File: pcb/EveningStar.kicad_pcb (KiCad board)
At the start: 2 copper layers, 9 parts, among them Q1 SQ2308CES-T1_GE3, U3 ISO6721RBD, U4 ESP32-C6-MINI-1, U5 LMR16010, U6 TLV803S, U7 W5500

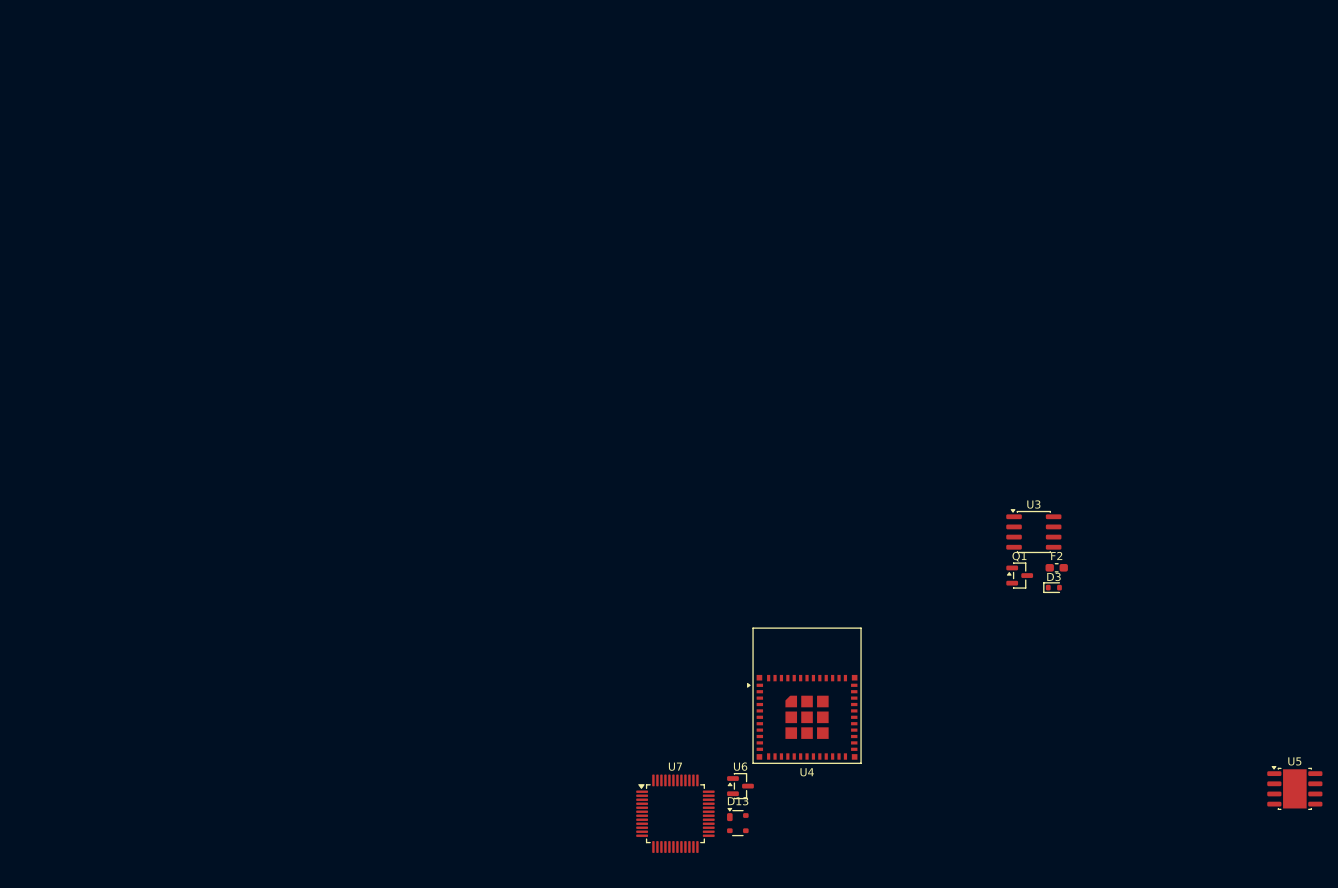
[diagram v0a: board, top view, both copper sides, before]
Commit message: feat: update compoents with lcsc parts
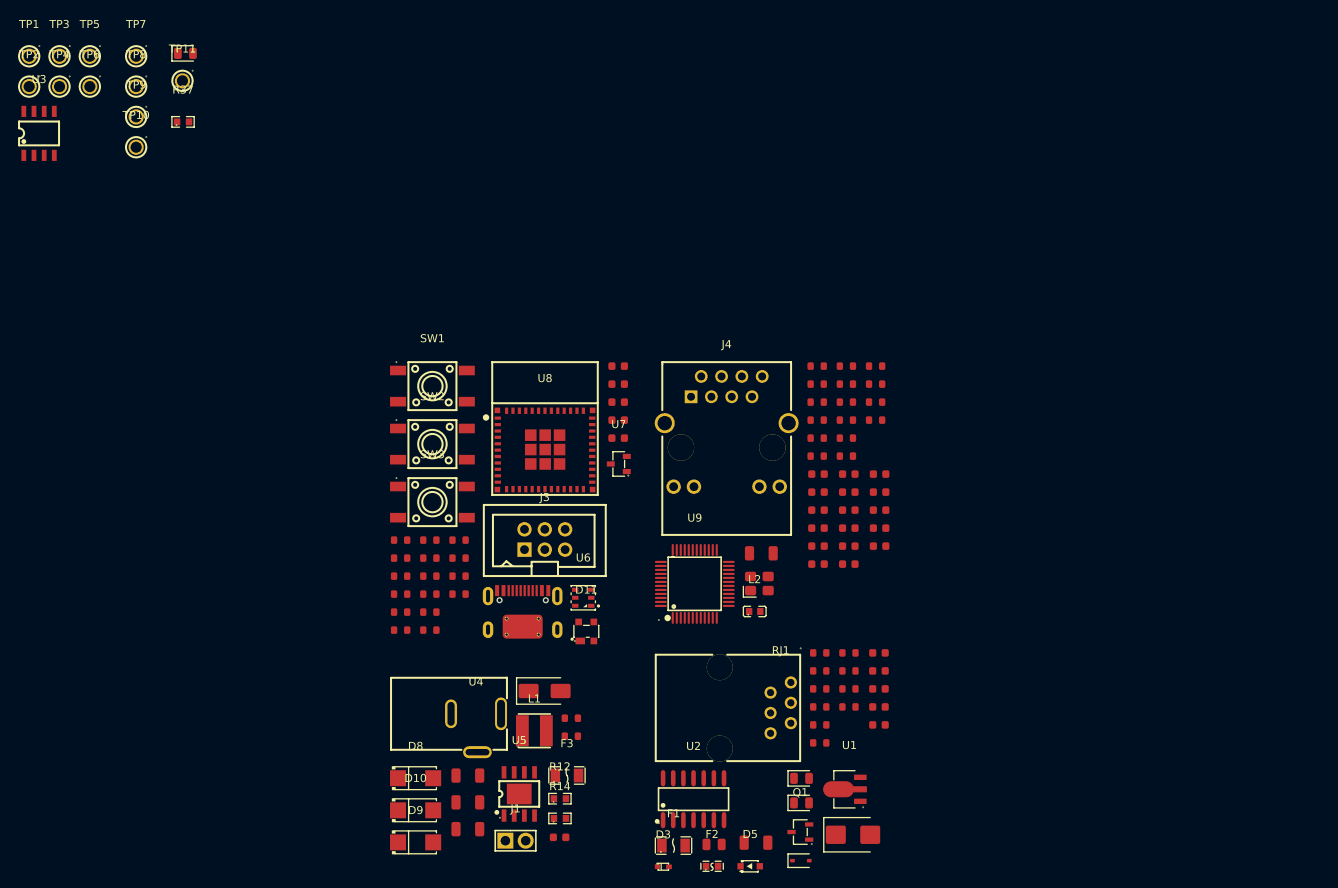
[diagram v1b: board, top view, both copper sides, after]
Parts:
- removed D13: PRTR5V0U2X, Package_TO_SOT_SMD:SOT-143
- added C1: 10uF, PCM_JLCPCB:C_1206, F.Cu at (92.2, 99.7)
- added C10: 100nF, PCM_JLCPCB:C_0603, F.Cu at (67.7, 99.0)
- added C11: 47uF, PCM_JLCPCB:C_1206, F.Cu at (56.2, 98.0)
- added C12: 100nF, PCM_JLCPCB:C_0603, F.Cu at (75.0, 44.6)
- added C13: 100nF, PCM_JLCPCB:C_0603, F.Cu at (75.0, 40.1)
- added C14: 100nF, PCM_JLCPCB:C_0603, F.Cu at (75.0, 42.4)
- added C15: 10uF, PCM_JLCPCB:C_0603, F.Cu at (75.0, 49.1)
- added C16: 100nF, PCM_JLCPCB:C_0603, F.Cu at (75.0, 46.9)
- added C17: 18pF, PCM_JLCPCB:C_0603, F.Cu at (100.0, 55.9)
- added C18: 18pF, PCM_JLCPCB:C_0603, F.Cu at (100.0, 53.6)
- added C19: 10uF, PCM_JLCPCB:C_0603, F.Cu at (107.7, 62.6)
- added C2: 330nF, PCM_JLCPCB:C_0805, F.Cu at (87.0, 99.9)
- added C20: 100nF, PCM_JLCPCB:C_0603, F.Cu at (100.0, 62.6)
- added C21: 1nF, PCM_JLCPCB:C_1206, F.Cu at (92.9, 63.5)
- added C22: 100nF, PCM_JLCPCB:C_0603, F.Cu at (100.0, 64.9)
- added C23: 10nF, PCM_JLCPCB:C_0603, F.Cu at (107.7, 55.9)
- added C24: 100nF, PCM_JLCPCB:C_0603, F.Cu at (103.8, 53.6)
- added C25: 4.7uF, PCM_JLCPCB:C_0603, F.Cu at (103.8, 55.9)
- added C26: 100nF, PCM_JLCPCB:C_0603, F.Cu at (103.8, 58.1)
- added C27: 100nF, PCM_JLCPCB:C_0603, F.Cu at (103.8, 62.6)
- added C28: 100nF, PCM_JLCPCB:C_0603, F.Cu at (103.8, 64.9)
- added C29: 10nF, PCM_JLCPCB:C_0603, F.Cu at (107.7, 60.4)
- added C3: 100nF, PCM_JLCPCB:C_0603, F.Cu at (107.6, 78.2)
- added C30: 100nF, PCM_JLCPCB:C_0603, F.Cu at (107.7, 53.6)
- added C31: 6.8nF, PCM_JLCPCB:C_0603, F.Cu at (107.7, 58.1)
- added C32: 6.8nF, PCM_JLCPCB:C_0603, F.Cu at (100.0, 60.4)
- added C33: 10uF, PCM_JLCPCB:C_0603, F.Cu at (103.8, 60.4)
- added C34: 22nF, PCM_JLCPCB:C_0603, F.Cu at (100.0, 58.1)
- added C4: 10uF, PCM_JLCPCB:C_0603, F.Cu at (107.6, 76.0)
- added C5: 100nF, PCM_JLCPCB:C_0603, F.Cu at (107.6, 80.5)
- added C6: 100nF, PCM_JLCPCB:C_0603, F.Cu at (107.6, 85.0)
- added C7: 100nF, PCM_JLCPCB:C_0603, F.Cu at (107.6, 82.7)
- added C8: 2.2uF, PCM_JLCPCB:C_1206, F.Cu at (56.2, 91.3)
- added C9: 2.2uF, PCM_JLCPCB:C_1206, F.Cu at (56.2, 94.7)
- added D1: SMBJ30CA, PCM_JLCPCB:D_SMB, F.Cu at (104.4, 98.7)
- added D10: STPS1H100A, EasyEDA:SMA_L4.3-W2.6-LS5.2-RD, F.Cu at (49.7, 95.6)
- added D11: PRTR5V0U2X_C2827688, EasyEDA:SOT-143-4_L2.9-W1.3-P1.92-LS2.4-BL, F.Cu at (71.0, 73.3)
- added D12: White, PCM_JLCPCB:D_0805, F.Cu at (20.9, 1.03)
- added D2: B16WS, PCM_JLCPCB:D_SOD-323, F.Cu at (97.9, 101.9)
- added D4: Red, PCM_JLCPCB:D_0805, F.Cu at (97.9, 94.7)
- added D5: BZX384-B5V1,115, EasyEDA:SOD-323_L1.7-W1.3-LS2.5-RD, F.Cu at (91.5, 102.6)
- added D6: Green, PCM_JLCPCB:D_0805, F.Cu at (97.9, 91.7)
- added D7: SMAJ28CA, PCM_JLCPCB:D_SMA, F.Cu at (65.8, 80.7)
- added D8: STPS1H100A, EasyEDA:SMA_L4.3-W2.6-LS5.2-RD, F.Cu at (49.7, 91.6)
- added D9: STPS1H100A, EasyEDA:SMA_L4.3-W2.6-LS5.2-RD, F.Cu at (49.7, 99.7)
- added F1: BSMD1206C-0500T, EasyEDA:F1206, F.Cu at (81.9, 100.1)
- added F3: 1A, EasyEDA:F1206, F.Cu at (68.6, 91.3)
- added J1: 3V3_JMP, EasyEDA:HDR-TH_2P-P2.54-V-M, F.Cu at (62.2, 99.5)
- added J2: Connector, USB-TYPE-C-16P, PCM_JLCPCB:TYPE-C-SMD_HX-TYPE-C-16PIN, F.Cu at (63.1, 70.7)
- added J3: ESPPROG, EasyEDA:IDC-TH_6P-P2.54-V-R2-C3-S2.54, F.Cu at (65.8, 61.8)
- added J4: RJ45_Hanrun_HR911105A_Horizontal, EasyEDA:RJ45-TH_HR911105A, F.Cu at (88.6, 48.3)
- added L1: 10uH, EasyEDA:IND-SMD_L4.0-W4.0_FNR40XXS, F.Cu at (64.5, 85.7)
- added L2: BLM18PG121SN1D_C14709, EasyEDA:L0603, F.Cu at (92.1, 70.8)
- added R1: 100Ω, PCM_JLCPCB:R_0603, F.Cu at (100.2, 87.2)
- added R10: 10kΩ, PCM_JLCPCB:R_0603, F.Cu at (103.9, 80.5)
- added R11: 10kΩ, PCM_JLCPCB:R_0603, F.Cu at (69.2, 84.1)
- added R12: 34.8k, EasyEDA:R0603, F.Cu at (67.7, 94.2)
- added R13: 100kΩ, PCM_JLCPCB:R_0603, F.Cu at (69.2, 86.4)
- added R14: 29.4k, EasyEDA:R0603, F.Cu at (67.7, 96.7)
- added R15: 10kΩ, PCM_JLCPCB:R_0603, F.Cu at (47.8, 73.1)
- added R16: 10kΩ, PCM_JLCPCB:R_0603, F.Cu at (51.5, 61.9)
- added R17: 10kΩ, PCM_JLCPCB:R_0603, F.Cu at (51.5, 70.9)
- added R18: 5.1kΩ, PCM_JLCPCB:R_0603, F.Cu at (47.8, 61.9)
- added R19: 5.1kΩ, PCM_JLCPCB:R_0603, F.Cu at (47.8, 64.1)
- added R2: 1MΩ, PCM_JLCPCB:R_0603, F.Cu at (100.2, 76.0)
- added R20: 10kΩ, PCM_JLCPCB:R_0603, F.Cu at (51.5, 73.1)
- added R21: 10kΩ, PCM_JLCPCB:R_0603, F.Cu at (55.1, 61.9)
- added R22: 220Ω, PCM_JLCPCB:R_0603, F.Cu at (47.8, 66.4)
- added R23: 33Ω, PCM_JLCPCB:R_0603, F.Cu at (47.8, 68.6)
- added R24: 33Ω, PCM_JLCPCB:R_0603, F.Cu at (47.8, 70.9)
- added R25: 33Ω, PCM_JLCPCB:R_0603, F.Cu at (51.5, 64.1)
- added R26: 33Ω, PCM_JLCPCB:R_0603, F.Cu at (51.5, 66.4)
- added R27: 33Ω, PCM_JLCPCB:R_0603, F.Cu at (51.5, 68.6)
- added R28: 10kΩ, PCM_JLCPCB:R_0603, F.Cu at (55.1, 64.1)
- added R29: 10kΩ, PCM_JLCPCB:R_0603, F.Cu at (55.1, 66.4)
- added R3: 100kΩ, PCM_JLCPCB:R_0603, F.Cu at (103.9, 78.2)
- added R30: 10kΩ, PCM_JLCPCB:R_0603, F.Cu at (55.1, 68.6)
- added R31: 1MΩ, PCM_JLCPCB:R_0603, F.Cu at (99.9, 40.1)
- added R32: 0Ω, PCM_JLCPCB:R_0603, F.Cu at (99.9, 42.4)
- added R33: 33Ω, PCM_JLCPCB:R_0603, F.Cu at (99.9, 44.6)
- added R34: 33Ω, PCM_JLCPCB:R_0603, F.Cu at (99.9, 46.9)
- added R35: 33Ω, PCM_JLCPCB:R_0603, F.Cu at (99.9, 49.1)
- added R36: 33Ω, PCM_JLCPCB:R_0603, F.Cu at (99.9, 51.4)
- added R37: 12.4k, EasyEDA:R0603, F.Cu at (20.6, 9.60)
- added R38: 49.9Ω, PCM_JLCPCB:R_0603, F.Cu at (103.5, 51.4)
- added R39: 10kΩ, PCM_JLCPCB:R_0603, F.Cu at (107.2, 42.4)
- added R4: 2MΩ, PCM_JLCPCB:R_0603, F.Cu at (100.2, 78.2)
- added R40: 10kΩ, PCM_JLCPCB:R_0603, F.Cu at (107.2, 44.6)
- added R41: 10kΩ, PCM_JLCPCB:R_0603, F.Cu at (107.2, 46.9)
- added R42: 49.9Ω, PCM_JLCPCB:R_0603, F.Cu at (103.5, 44.6)
- added R43: 49.9Ω, PCM_JLCPCB:R_0603, F.Cu at (103.5, 49.1)
- added R44: 49.9Ω, PCM_JLCPCB:R_0603, F.Cu at (103.5, 46.9)
- added R45: 10Ω, PCM_JLCPCB:R_0603, F.Cu at (107.2, 40.1)
- added R46: 330Ω, PCM_JLCPCB:R_0603, F.Cu at (103.5, 40.1)
- added R47: 330Ω, PCM_JLCPCB:R_0603, F.Cu at (103.5, 42.4)
- added R5: 100Ω, PCM_JLCPCB:R_0603, F.Cu at (100.2, 80.5)
- added R6: 330Ω, PCM_JLCPCB:R_0603, F.Cu at (100.2, 82.7)
- added R7: 100kΩ, PCM_JLCPCB:R_0603, F.Cu at (103.9, 76.0)
- added R8: 330Ω, PCM_JLCPCB:R_0603, F.Cu at (100.2, 85.0)
- added R9: 10kΩ, PCM_JLCPCB:R_0603, F.Cu at (103.9, 82.7)
- added RJ1: 5301-6P6C, EasyEDA:RJ45-TH_5301-6P6C, F.Cu at (95.3, 82.8)
- added SW1: RST_SW, EasyEDA:KEY-SMD_4P-L6.0-W6.0-P3.90-LS9.0, F.Cu at (51.8, 42.6)
- added SW2: BOOT_SW, EasyEDA:KEY-SMD_4P-L6.0-W6.0-P3.90-LS9.0, F.Cu at (51.8, 49.9)
- added SW3: CFG_SW, EasyEDA:KEY-SMD_4P-L6.0-W6.0-P3.90-LS9.0, F.Cu at (51.8, 57.1)
- added TP1: TestPoint, EasyEDA:TEST-TH_BD2.54-P1.4_BLACK, F.Cu at (1.40, 1.40)
- added TP10: TestPoint, EasyEDA:TEST-TH_BD2.54-P1.4_BLACK, F.Cu at (14.8, 12.8)
- added TP11: TestPoint, EasyEDA:TEST-TH_BD2.54-P1.4_BLACK, F.Cu at (20.6, 4.46)
- added TP2: TestPoint, EasyEDA:TEST-TH_BD2.54-P1.4_BLACK, F.Cu at (1.40, 5.18)
- added TP3: TestPoint, EasyEDA:TEST-TH_BD2.54-P1.4_BLACK, F.Cu at (5.18, 1.40)
- added TP4: TestPoint, EasyEDA:TEST-TH_BD2.54-P1.4_BLACK, F.Cu at (5.18, 5.18)
- added TP5: TestPoint, EasyEDA:TEST-TH_BD2.54-P1.4_BLACK, F.Cu at (8.97, 1.40)
- added TP6: TestPoint, EasyEDA:TEST-TH_BD2.54-P1.4_BLACK, F.Cu at (8.97, 5.18)
- added TP7: TestPoint, EasyEDA:TEST-TH_BD2.54-P1.4_BLACK, F.Cu at (14.8, 1.40)
- added TP8: TestPoint, EasyEDA:TEST-TH_BD2.54-P1.4_BLACK, F.Cu at (14.8, 5.18)
- added TP9: TestPoint, EasyEDA:TEST-TH_BD2.54-P1.4_BLACK, F.Cu at (14.8, 8.97)
- added U1: AMS1117S-5.0, EasyEDA:SOT-89-3_L4.5-W2.5-P1.50-LS4.2-BR, F.Cu at (103.9, 93.0)
- added U2: SN74HC132DR, EasyEDA:SOIC-14_L8.7-W3.9-P1.27-LS6.0-BL, F.Cu at (84.4, 94.3)
- added U8: ESP32-C6-MINI-1, EasyEDA:WIFIM-SMD_61P-L16.6-W13.2-P0.80-ESP32-C6-MINI-1-N4, F.Cu at (65.9, 50.6)
- added U9: W5500, EasyEDA:LQFP-48_L7.0-W7.0-P0.50-LS9.0-BL, F.Cu at (84.6, 67.3)
- added Y1: 25MHz, PCM_JLCPCB:OSC-SMD_4P-L3.2-W2.5-BL, F.Cu at (92.7, 67.3)
- D3: footprint Diode_SMD:D_SOD-523 -> EasyEDA:SOD-523F_L1.2-W0.8-LS1.7-RD
- F2: footprint Fuse:Fuse_0603_1608Metric_Pad1.05x0.95mm_HandSolder -> EasyEDA:F0603
- Q1: value SQ2308CES-T1_GE3 -> SQ2308CES-T1_GE3-HXY; footprint Package_TO_SOT_SMD:SOT-23 -> EasyEDA:SOT-23-3_L3.0-W1.7-P0.95-LS2.9-BR
- U3: value ISO6721RBD -> ISO6721RBDR; footprint Package_SO:SOIC-8_3.9x4.9mm_P1.27mm -> EasyEDA:SOP-8_L4.9-W3.9-P1.27-LS6.0-BL_ISO6721RBDR
- U4: value ESP32-C6-MINI-1 -> DC-005H-D020; footprint RF_Module:ESP32-C6-MINI-1 -> EasyEDA:DC-IN-TH_G-SWITCH_DC-005H-D020
- U5: footprint Package_SO:Texas_R-PDSO-G8_EP2.95x4.9mm_Mask2.4x3.1mm -> EasyEDA:SOPOWERPAD-8_L4.9-W3.9-P1.27-LS6.0-BL-EP
- U6: value TLV803S -> AHT20_C2757850; footprint Package_TO_SOT_SMD:SOT-23 -> EasyEDA:SENSOR-SMD_L3.0-W3.0-P1.00-BR
- U7: value W5500 -> TLV803SDBZR; footprint Package_QFP:LQFP-48_7x7mm_P0.5mm -> EasyEDA:SOT-23-3_L2.9-W1.3-P1.90-LS2.4-BR
- moved U3 134.0 mm to (2.62, 11.0)
- moved U5 97.0 mm to (62.6, 93.6)
- moved D3 60.0 mm to (80.7, 102.7)
- moved F2 57.0 mm to (86.8, 102.6)
- moved U7 44.3 mm to (75.1, 52.4)
- moved Q1 42.2 mm to (97.8, 98.4)
- moved U4 41.4 mm to (57.2, 86.0)
- moved U6 30.7 mm to (70.7, 69.1)
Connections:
- Q1 pad 2: Net-(Q1-D) -> GND_ISO
- Q1 pad 3: GND_ISO -> Net-(Q1-D)
- U3 pad 6: /meterbus_frontend/MB_WRITE -> MB_WRITE
- U3 pad 7: /meterbus_frontend/MB_READ -> MB_READ
- U3 pad 8: +3.3V -> +3V3
- U4 pad 1: GND -> Net-(F3-Pad1)
- U4 pad 3: +3V3 -> unconnected-(U4-Pad3)
- U6 pad 1: GND -> unconnected-(U6-NC-Pad1)
- U6 pad 2: /mcu/MCU_RESET -> +3V3
- U6 pad 3: Net-(U6-VIN) -> /mcu/SCL
- U7 pad 1: unconnected-(U7-TXN-Pad1) -> GND
- U7 pad 2: unconnected-(U7-TXP-Pad2) -> /mcu/MCU_RESET
- U7 pad 3: Net-(U7-AGND-Pad14) -> +3V3

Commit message: feat: layout meterbus frontend
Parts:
- added TP12: BUS, EasyEDA:TEST-TH_BD2.54-P1.4_BLACK, F.Cu at (-190.0, 48.0)
- added TP13: 5V_ISO, EasyEDA:TEST-TH_BD2.54-P1.4_BLACK, F.Cu at (-156.0, 28.0)
- added TP14: RX_MB, EasyEDA:TEST-TH_BD2.54-P1.4_BLACK, F.Cu at (-165.0, 54.0)
- added TP15: TX_MB, EasyEDA:TEST-TH_BD2.54-P1.4_BLACK, F.Cu at (-158.0, 54.0)
- added TP16: TX_MCU, EasyEDA:TEST-TH_BD2.54-P1.4_BLACK, F.Cu at (-134.0, 36.5)
- added TP17: RX_MCU, EasyEDA:TEST-TH_BD2.54-P1.4_BLACK, F.Cu at (-134.0, 24.5)
- D4: value Red -> TX
- D6: value Green -> RX
- TP1: value TestPoint -> BAT_ISO
- TP2: value TestPoint -> BAT_ISO_PROT
- TP3: value TestPoint -> GND_ISO
- TP4: value TestPoint -> BUS_PROT
- TP5: value TestPoint -> TX_GATE
- TP6: value TestPoint -> RX_DIV
- TP7: value TestPoint -> GND
- TP8: value TestPoint -> VIN
- TP9: value TestPoint -> DCDC_FB
- moved J4 302.3 mm to (390.9, 48.0), turned to 90 degrees
- moved D1 285.7 mm to (-174.5, 36.5)
- moved RJ1 280.8 mm to (-181.9, 38.4)
- moved R1 280.2 mm to (-177.0, 46.5)
- moved R3 279.3 mm to (-174.0, 49.5), turned to 90 degrees
- moved Q1 279.2 mm to (-177.1, 49.5)
- moved D2 278.2 mm to (-171.5, 32.5), turned to 180 degrees
- moved C7 276.4 mm to (-165.0, 37.0), turned to 180 degrees
- moved R4 276.4 mm to (-173.5, 40.0), turned to 180 degrees
- moved R2 275.6 mm to (-173.5, 44.0)
- moved U9 273.5 mm to (357.2, 46.2)
- moved R5 273.4 mm to (-171.5, 50.5)
- moved U1 272.5 mm to (-162.0, 33.6), turned to 90 degrees
- moved D5 271.9 mm to (-173.5, 42.0), turned to 180 degrees
- moved R8 271.2 mm to (-168.5, 48.0)
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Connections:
- C6 pad 2: GND_ISO -> GND
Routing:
- net GND_ISO: track 0.00 -> 117.6 mm, vias 0 -> 5
- net +5V_ISO: track 0.00 -> 35.8 mm
- net Net-(U3-INA): track 0.00 -> 34.6 mm, vias 0 -> 2
- net Net-(D5-C): track 0.00 -> 26.4 mm, vias 0 -> 1
- net Net-(U3-OUTB): track 0.00 -> 23.4 mm
- net Net-(F2-Pad1): track 0.00 -> 19.6 mm
- net Net-(D3-Cathode): track 0.00 -> 15.9 mm
- net Net-(R5-Pad2): track 0.00 -> 13.6 mm
- net +BATT_ISO: track 0.00 -> 12.0 mm
- net +PROT_BATT_ISO: track 0.00 -> 11.6 mm
- net Net-(Q1-G): track 0.00 -> 9.28 mm
- net Net-(D1-Pad2): track 0.00 -> 6.91 mm
- net Net-(Q1-D): track 0.00 -> 3.11 mm
- net Net-(U2-Pad3): track 0.00 -> 2.54 mm
- net Net-(D6-Pad2): track 0.00 -> 1.74 mm
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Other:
- board text added: "MeterBus Frontend"
